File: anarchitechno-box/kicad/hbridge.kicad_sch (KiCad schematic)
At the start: 16 parts, among them U11 DRV8243SQDGQRQ1

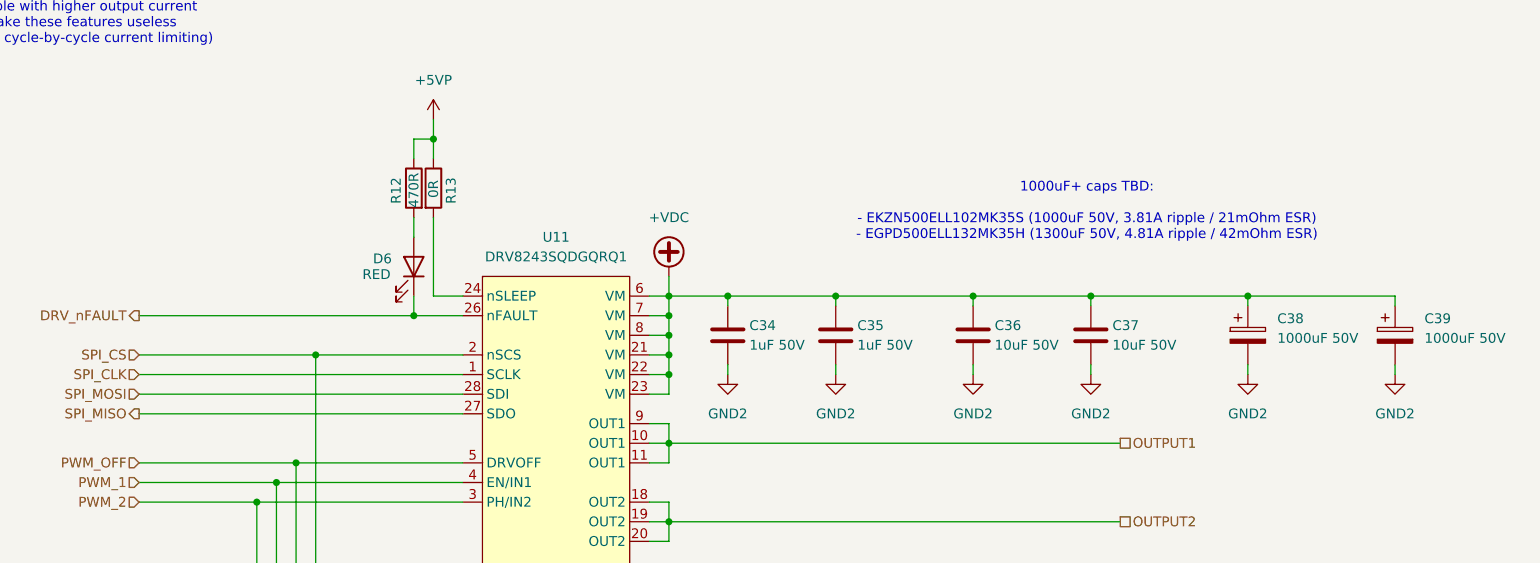
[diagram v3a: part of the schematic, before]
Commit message: Schematic & PCB changes: - Cleaned up unnecessary electrolytic input capacitor flyback - Removed dual diode rectification on 5V, increased output capacitors - Feedback resistors DC/DCs set, enlarged for JLC basic parts - Sweep through schematic to consolidate caps to JLC basic parts (see list schematic front page) - Midi OUTPUT added (please check schematic) - Wiznet W5500 schematic reworked to RJ45 reference schematic: https://docs.wiznet.io/assets/files/w5500_sch_v110_use_mag_-dfff8bbb103d13be4f25cd2b2f8b950d.pdf - Replaced ethernet jack to HR911105A - Crystals chosen for W5500 and RP2350B (according to reference), 15pF load caps. - RS485 driver changed to SP3485EN for 3.3V operation - Replaced RS485 bus connectors with 2x RJ45s for passthrough - Groove connector replaced with JST XH 2mm - Added LCSC part numbers for various components in the schematic
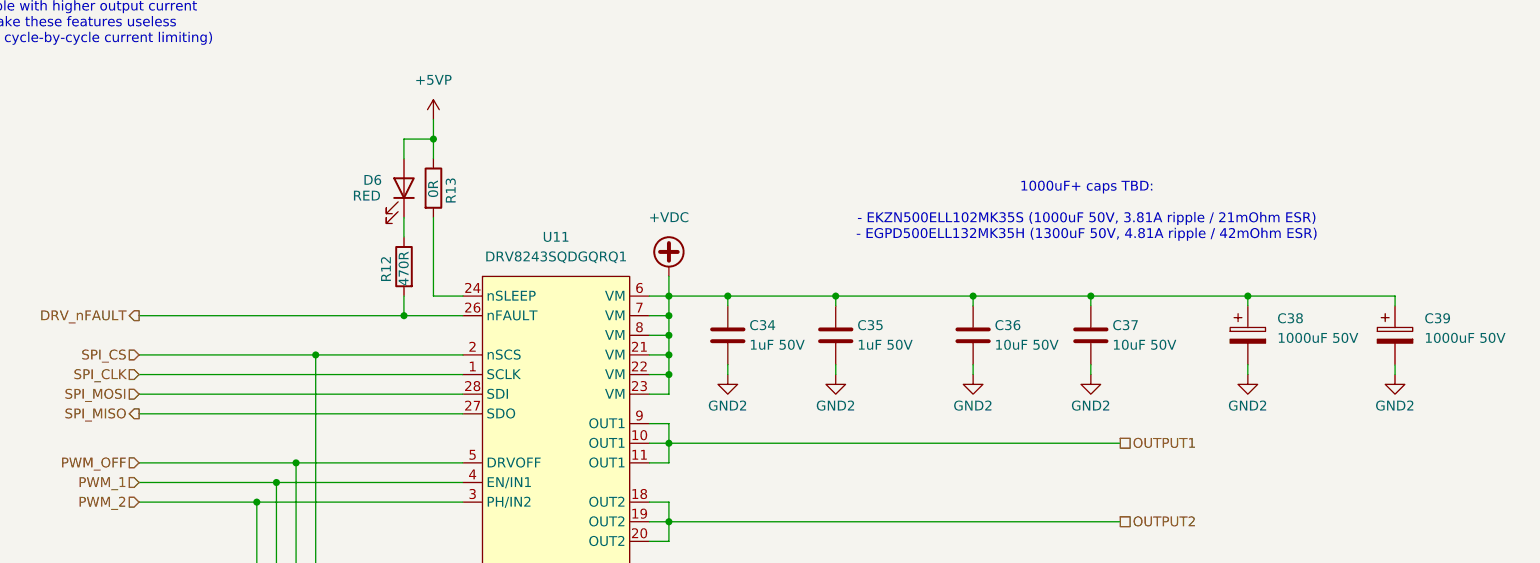
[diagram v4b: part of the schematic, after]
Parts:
- C34, C35: LCSC Part (none) -> C15849
- C36, C37: LCSC Part (none) -> C13585
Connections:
- net +5VP: now also D6.2 (A); no longer R12.1
- net DRV_nFAULT: now also R12.2; no longer D6.1 (K)
- new net: D6.1 (K), R12.1
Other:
- moved on the sheet: D6, R12
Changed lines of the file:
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@@
-	)
-	(junction
-		(at 111.76 69.85)
-		(diameter 0)
-		(color 0 0 0 0)
 	)
 	(junction
@@
 	)
 	(junction
+		(at 110.49 69.85)
+		(diameter 0)
+		(color 0 0 0 0)
+	)
+	(junction
 		(at 152.4 67.31)
 		(diameter 0)
@@
 	(wire
 		(pts
-			(xy 111.76 49.53) (xy 111.76 46.99)
-		)
-		(stroke
-			(width 0)
-			(type default)
-		)
-	)
-	(wire
-		(pts
 			(xy 144.78 83.82) (xy 144.78 86.36)
 		)
@@
 	(wire
 		(pts
+			(xy 110.49 69.85) (xy 118.11 69.85)
+		)
+		(stroke
+			(width 0)
+			(type default)
+		)
+	)
+	(wire
+		(pts
 			(xy 144.78 96.52) (xy 203.2 96.52)
 		)
@@
 	(wire
 		(pts
-			(xy 118.11 69.85) (xy 111.76 69.85)
-		)
-		(stroke
-			(width 0)
-			(type default)
-		)
-	)
-	(wire
-		(pts
 			(xy 238.76 67.31) (xy 219.71 67.31)
 		)
@@
 	(wire
 		(pts
+			(xy 110.49 49.53) (xy 110.49 46.99)
+		)
+		(stroke
+			(width 0)
+			(type default)
+		)
+	)
+	(wire
+		(pts
 			(xy 118.11 104.14) (xy 114.3 104.14)
 		)
@@
 	(wire
 		(pts
-			(xy 111.76 69.85) (xy 111.76 67.31)
-		)
-		(stroke
-			(width 0)
-			(type default)
-		)
-	)
-	(wire
-		(pts
 			(xy 99.06 110.49) (xy 99.06 74.93)
 		)
@@
 	(wire
 		(pts
-			(xy 76.2 69.85) (xy 111.76 69.85)
+			(xy 76.2 69.85) (xy 110.49 69.85)
+		)
+		(stroke
+			(width 0)
+			(type default)
+		)
+	)
+	(wire
+		(pts
+			(xy 110.49 57.15) (xy 110.49 59.69)
 		)
 		(stroke
@@
 	(wire
 		(pts
-			(xy 111.76 59.69) (xy 111.76 57.15)
-		)
-		(stroke
-			(width 0)
-			(type default)
-		)
-	)
-	(wire
-		(pts
 			(xy 144.78 111.76) (xy 144.78 114.3)
 		)
@@
 	(wire
 		(pts
+			(xy 110.49 46.99) (xy 114.3 46.99)
+		)
+		(stroke
+			(width 0)
+			(type default)
+		)
+	)
+	(wire
+		(pts
 			(xy 142.24 119.38) (xy 144.78 119.38)
 		)
@@
 	(wire
 		(pts
+			(xy 110.49 67.31) (xy 110.49 69.85)
+		)
+		(stroke
+			(width 0)
+			(type default)
+		)
+	)
+	(wire
+		(pts
 			(xy 142.24 116.84) (xy 144.78 116.84)
 		)
@@
 		(pts
 			(xy 144.78 77.47) (xy 144.78 74.93)
-		)
-		(stroke
-			(width 0)
-			(type default)
-		)
-	)
-	(wire
-		(pts
-			(xy 111.76 46.99) (xy 114.3 46.99)
 		)
 		(stroke
@@
 		(on_board yes)
 		(dnp no)
-		(fields_autoplaced yes)
 		(property "Reference" "#PWR076"
 			(at 199.39 83.82 0)
@@
 		)
 		(property "Value" "GND2"
-			(at 199.39 82.55 0)
+			(at 199.39 81.534 0)
 			(effects
 				(font
@@
 			)
 		)
+		(property "LCSC Part" "C13585"
+			(at 199.39 72.39 0)
+			(effects
+				(font
+					(size 1.27 1.27)
+				)
+				(hide yes)
+			)
+		)
 		(pin "2"
 		)
@@
 		(on_board yes)
 		(dnp no)
-		(fields_autoplaced yes)
 		(property "Reference" "#PWR077"
 			(at 219.71 83.82 0)
@@
 		)
 		(property "Value" "GND2"
-			(at 219.71 82.55 0)
+			(at 219.71 81.534 0)
 			(effects
 				(font
@@
 		)
 		(property "Description" "Unpolarized capacitor"
+			(at 152.4 72.39 0)
+			(effects
+				(font
+					(size 1.27 1.27)
+				)
+				(hide yes)
+			)
+		)
+		(property "LCSC Part" "C15849"
 			(at 152.4 72.39 0)
 			(effects
@@
 	(symbol
 		(lib_id "Device:R")
-		(at 111.76 53.34 0)
+		(at 110.49 63.5 0)
 		(mirror y)
 		(unit 1)
@@
 		(dnp no)
 		(property "Reference" "R12"
-			(at 109.474 55.372 90)
+			(at 108.204 65.532 90)
 			(effects
 				(font
@@
 		)
 		(property "Value" "470R"
-			(at 111.76 55.88 90)
+			(at 110.49 66.04 90)
 			(effects
 				(font
@@
 		)
 		(property "Footprint" "Resistor_SMD:R_0402_1005Metric"
-			(at 113.538 53.34 90)
+			(at 112.268 63.5 90)
 			(effects
 				(font
@@
 		)
 		(property "Datasheet" "~"
-			(at 111.76 53.34 0)
+			(at 110.49 63.5 0)
 			(effects
 				(font
@@
 		)
 		(property "Description" "Resistor"
-			(at 111.76 53.34 0)
+			(at 110.49 63.5 0)
 			(effects
 				(font
@@
 		(on_board yes)
 		(dnp no)
-		(fields_autoplaced yes)
 		(property "Reference" "#PWR078"
 			(at 238.76 83.82 0)
@@
 		)
 		(property "Value" "GND2"
-			(at 238.76 82.55 0)
+			(at 238.76 81.534 0)
 			(effects
 				(font
@@
 		(on_board yes)
 		(dnp no)
-		(fields_autoplaced yes)
 		(property "Reference" "#PWR073"
 			(at 152.4 83.82 0)
@@
 		)
 		(property "Value" "GND2"
-			(at 152.4 82.55 0)
+			(at 152.4 81.534 0)
 			(effects
 				(font
@@
 			)
 		)
+		(property "LCSC Part" "C15849"
+			(at 166.37 72.39 0)
+			(effects
+				(font
+					(size 1.27 1.27)
+				)
+				(hide yes)
+			)
+		)
 		(pin "2"
 		)
@@
 		(on_board yes)
 		(dnp no)
-		(fields_autoplaced yes)
 		(property "Reference" "#PWR075"
 			(at 184.15 83.82 0)
@@
 		)
 		(property "Value" "GND2"
-			(at 184.15 82.55 0)
+			(at 184.15 81.534 0)
 			(effects
 				(font
@@
 		(on_board yes)
 		(dnp no)
-		(fields_autoplaced yes)
 		(property "Reference" "#PWR074"
 			(at 166.37 83.82 0)
@@
 		)
 		(property "Value" "GND2"
-			(at 166.37 82.55 0)
+			(at 166.37 81.534 0)
 			(effects
 				(font
@@
 			)
 		)
+		(property "LCSC Part" "C13585"
+			(at 184.15 72.39 0)
+			(effects
+				(font
+					(size 1.27 1.27)
+				)
+				(hide yes)
+			)
+		)
 		(pin "2"
 		)
@@
 	(symbol
 		(lib_id "Device:LED")
-		(at 111.76 63.5 270)
+		(at 110.49 53.34 270)
 		(mirror x)
 		(unit 1)
@@
 		(dnp no)
 		(property "Reference" "D6"
-			(at 107.696 62.484 90)
+			(at 106.426 52.324 90)
 			(effects
 				(font
@@
 		)
 		(property "Value" "RED"
-			(at 106.934 64.516 90)
+			(at 105.664 54.356 90)
 			(effects
 				(font
@@
 		)
 		(property "Footprint" "LED_SMD:LED_0603_1608Metric"
-			(at 111.76 63.5 0)
+			(at 110.49 53.34 0)
 			(effects
 				(font
@@
 		)
 		(property "Datasheet" "~"
-			(at 111.76 63.5 0)
+			(at 110.49 53.34 0)
 			(effects
 				(font
@@
 		)
 		(property "Description" "Light emitting diode"
-			(at 111.76 63.5 0)
+			(at 110.49 53.34 0)
 			(effects
 				(font
@@
 		)
 		(property "Sim.Pins" "1=K 2=A"
-			(at 111.76 63.5 0)
-			(effects
-				(font
+			(at 110.49 53.34 0)
+			(effects
+				(font

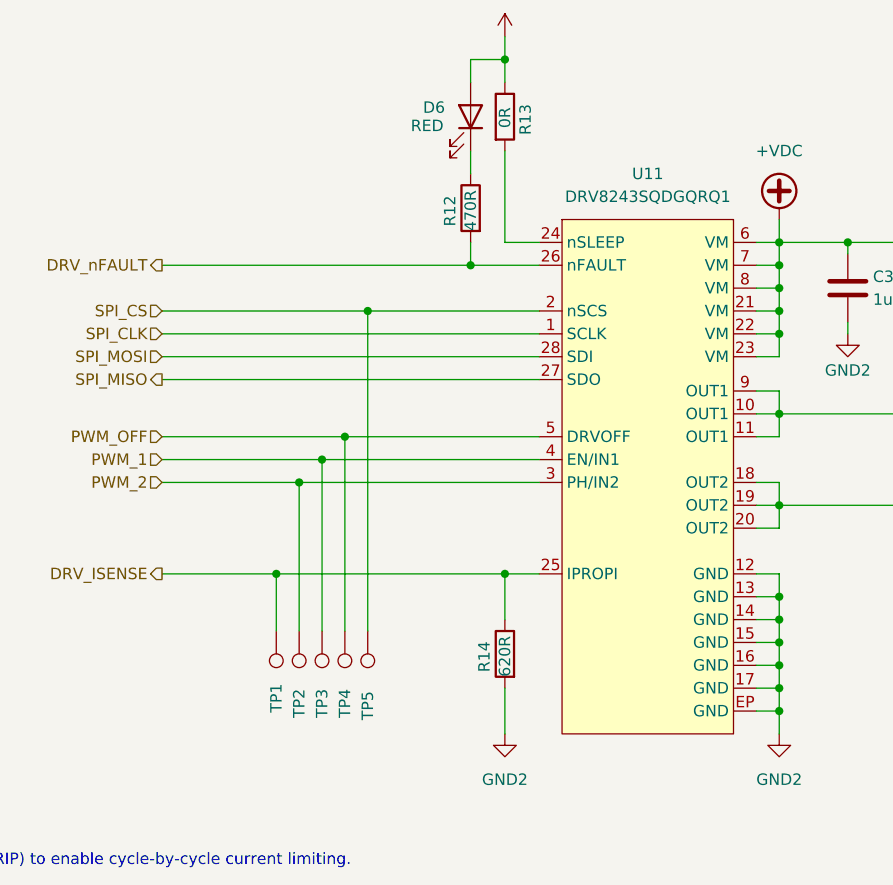
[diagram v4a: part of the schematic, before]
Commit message: - Thermische berekening DRV8245 vs losse transistors - DRV8245 package gecorrigeerd naar TSSOP-28 - Layout aangepast om grotere package te passen - 1x GND output per kanaal - Waarschijnlijk geen 140mm fan nodig => print weer gekropmen - RS485 power line gefixed (3.3V vs 3V3P) - Kleine BOM en I/O wijzigingen tbv layout
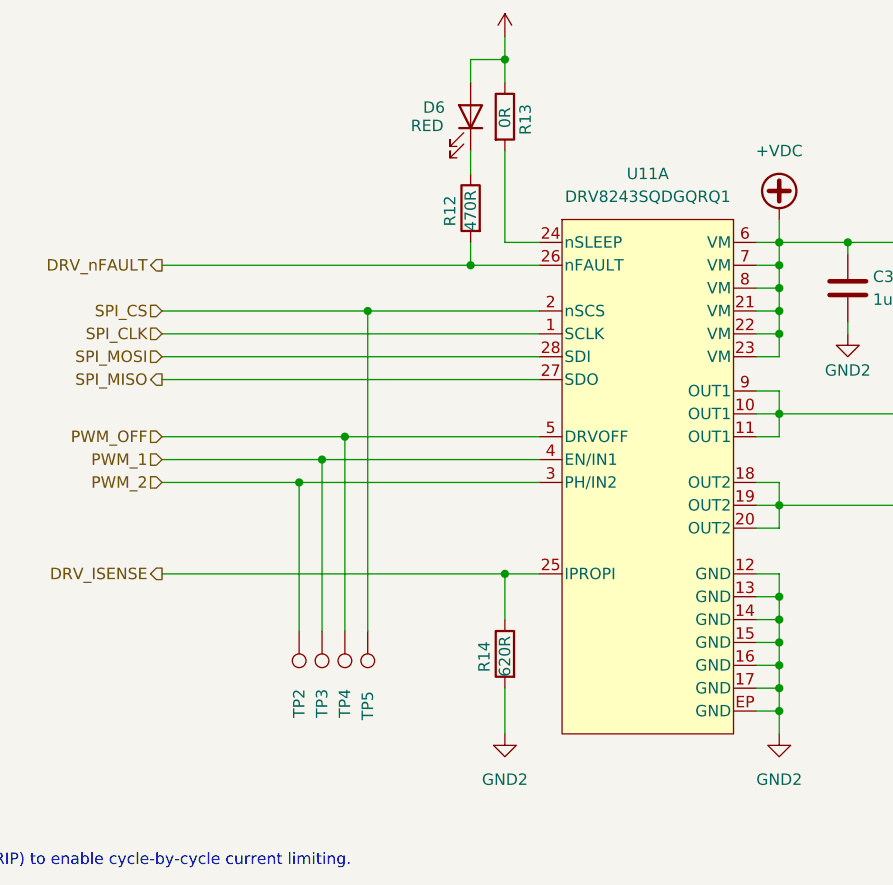
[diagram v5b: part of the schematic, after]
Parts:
- removed TP1: TestPoint, TestPoint:TestPoint_Pad_D1.0mm, symbol Connector:TestPoint
- U11: footprint parts:TI_HVSSOP-28 -> parts:TI_HTSSOP-28-M; symbol parts:DRV8243SQDGQRQ1 -> parts:DRV8245SQPWPRQ1; MPN DRV8243SQDGQRQ1 -> DRV8245SQPWPRQ1
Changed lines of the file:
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@@
-	)
-	(junction
-		(at 88.9 104.14)
-		(diameter 0)
-		(color 0 0 0 0)
 	)
 	(junction
@@
 	(wire
 		(pts
-			(xy 88.9 110.49) (xy 88.9 104.14)
-		)
-		(stroke
-			(width 0)
-			(type default)
-		)
-	)
-	(wire
-		(pts
 			(xy 144.78 111.76) (xy 144.78 114.3)
 		)
@@
 	(wire
 		(pts
-			(xy 88.9 104.14) (xy 114.3 104.14)
-		)
-		(stroke
-			(width 0)
-			(type default)
-		)
-	)
-	(wire
-		(pts
 			(xy 152.4 67.31) (xy 166.37 67.31)
 		)
@@
 	(wire
 		(pts
-			(xy 76.2 104.14) (xy 88.9 104.14)
+			(xy 76.2 104.14) (xy 114.3 104.14)
 		)
 		(stroke
@@
 	)
 	(symbol
-		(lib_id "parts:DRV8243SQDGQRQ1")
+		(lib_id "parts:DRV8245SQPWPRQ1")
 		(at 120.65 64.77 0)
 		(unit 1)
@@
 			)
 		)
-		(property "Footprint" "parts:TI_HVSSOP-28"
+		(property "Footprint" "parts:TI_HTSSOP-28-M"
+			(at 130.048 125.222 0)
+			(effects
+				(font
+					(size 1.27 1.27)
+					(italic yes)
+				)
+				(hide yes)
+			)
+		)
+		(property "Datasheet" "https://www.ti.com/lit/gpn/drv8245-q1"
+			(at 130.048 125.222 0)
+			(effects
+				(font
+					(size 1.27 1.27)
+					(italic yes)
+				)
+				(hide yes)
+			)
+		)
+		(property "Description" "Automotive H-Bridge Driver with Integrated Current Sense and Diagnostics"
 			(at 120.65 64.77 0)
 			(effects
@@
 			)
 		)
-		(property "Datasheet" "https://www.ti.com/lit/ds/symlink/drv8243-q1.pdf"
-			(at 146.05 126.746 0)
-			(effects
-				(font
-					(size 1.27 1.27)
-				)
-				(hide yes)
-			)
-		)
-		(property "Description" "Automotive H-Bridge Driver with Integrated Current Sense and Diagnostics"
-			(at 157.226 129.286 0)
-			(effects
-				(font
-					(size 1.27 1.27)
-				)
-				(hide yes)
-			)
-		)
-		(property "MPN" "DRV8243SQDGQRQ1"
-			(at 130.302 124.46 0)
+		(property "MPN" "DRV8245SQPWPRQ1"
+			(at 130.048 125.222 0)
 			(effects
 				(font
@@
 		)
 		(pin "21"
+		)
+		(pin "6"
+		)
+		(pin "7"
+		)
+		(pin "8"
+		)
+		(pin "21"
+		)
+		(pin "22"
+		)
+		(pin "23"
+		)
+		(pin "EPAD"
+		)
+		(pin "12"
+		)
+		(pin "13"
+		)
+		(pin "14"
+		)
+		(pin "15"
+		)
+		(pin "16"
+		)
+		(pin "17"
 		)
 		(instances
@@
 					(unit 1)
 				)
-			)
-		)
-	)
-	(symbol
-		(lib_id "Connector:TestPoint")
-		(at 88.9 110.49 180)
-		(unit 1)
-		(exclude_from_sim no)
-		(in_bom yes)
-		(on_board yes)
-		(dnp no)
-		(property "Reference" "TP1"
-			(at 88.9 116.332 90)
-			(effects
-				(font
-					(size 1.27 1.27)
-				)
-				(justify left)
-			)
-		)
-		(property "Value" "TestPoint"
-			(at 86.36 113.792 90)
-			(effects
-				(font
-					(size 1.27 1.27)
-				)
-				(hide yes)
-			)
-		)
-		(property "Footprint" "TestPoint:TestPoint_Pad_D1.0mm"
-			(at 83.82 110.49 0)
-			(effects
-				(font
-					(size 1.27 1.27)
-				)
-				(hide yes)
-			)
-		)
-		(property "Datasheet" "~"
-			(at 83.82 110.49 0)
-			(effects
-				(font
-					(size 1.27 1.27)
-				)
-				(hide yes)
-			)
-		)
-		(property "Description" "test point"
-			(at 88.9 110.49 0)
-			(effects
-				(font
-					(size 1.27 1.27)
-				)
-				(hide yes)
-			)
-		)
-		(pin "1"
-		)
-		(instances
-			(project "anarchytechnobox"
-				(path "/8c734c41-38ed-40fc-83bd-134786dcfb35/48f260d8-d62f-49a9-8985-05fca65ac6cb/0c0607e4-80d3-46ba-8adb-76563a900b03"
-					(reference "TP16")
-					(unit 1)
-				)
-				(path "/8c734c41-38ed-40fc-83bd-134786dcfb35/48f260d8-d62f-49a9-8985-05fca65ac6cb/ec360df5-fff7-49b0-afa3-93c9754653a9"
-					(reference "TP11")
-					(unit 1)
-				)
-				(path "/8c734c41-38ed-40fc-83bd-134786dcfb35/f97c65ed-bb3f-4eb8-a2c6-056cc510b5f8/0c0607e4-80d3-46ba-8adb-76563a900b03"
-					(reference "TP6")
-					(unit 1)
-				)
-				(path "/8c734c41-38ed-40fc-83bd-134786dcfb35/f97c65ed-bb3f-4eb8-a2c6-056cc510b5f8/ec360df5-fff7-49b0-afa3-93c9754653a9"
-					(reference "TP1")
-					(unit 1)
-				)

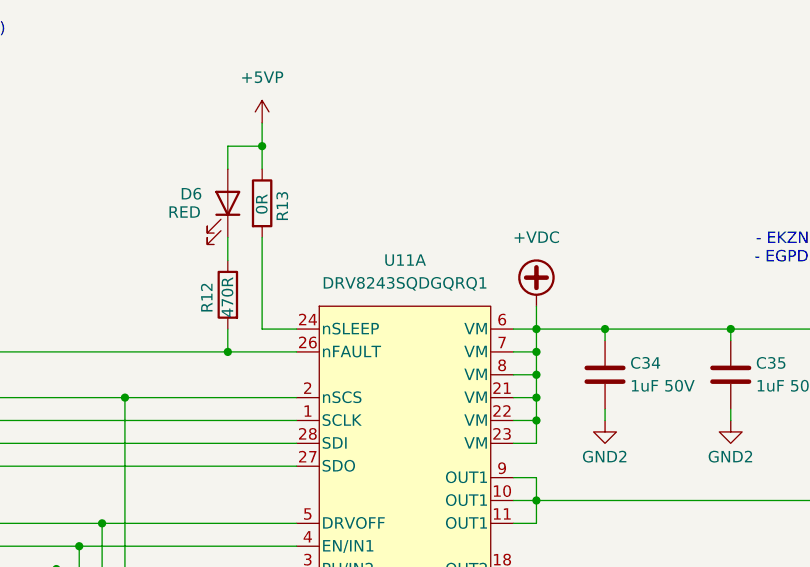
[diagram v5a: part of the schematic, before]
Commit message: BOM nagelopen, bestelklaar.
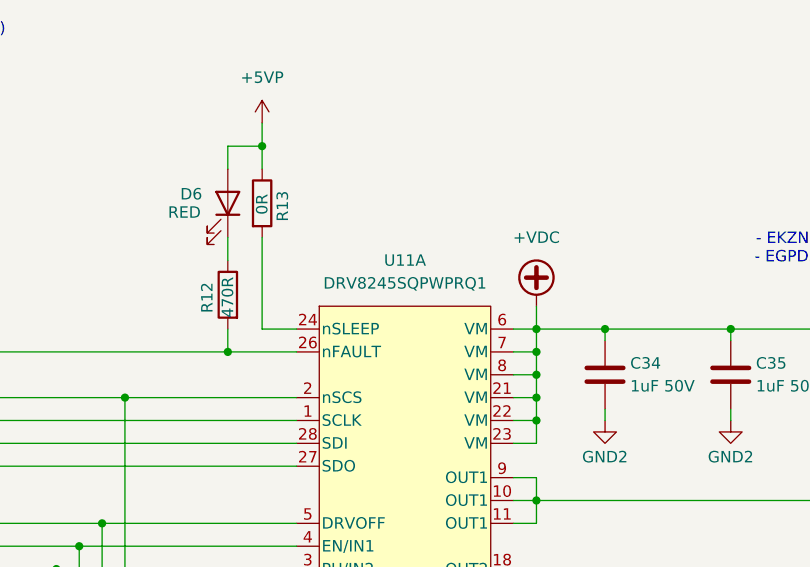
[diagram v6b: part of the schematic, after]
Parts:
- C38, C39: LCSC Part (none) -> C443023
- TP2, TP3, TP4, TP5: now left out of the parts list
- U11: value DRV8243SQDGQRQ1 -> DRV8245SQPWPRQ1; LCSC Part (none) -> C5672500
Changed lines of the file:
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@@
 			)
 		)
-		(property "Value" "DRV8243SQDGQRQ1"
+		(property "Value" "DRV8245SQPWPRQ1"
 			(at 130.175 62.23 0)
 			(effects
@@
 			)
 		)
+		(property "LCSC Part" "C5672500"
+			(at 120.65 64.77 0)
+			(effects
+				(font
+					(size 1.27 1.27)
+				)
+				(hide yes)
+			)
+		)
 		(pin "19"
 		)
@@
 		(unit 1)
 		(exclude_from_sim no)
-		(in_bom yes)
+		(in_bom no)
 		(on_board yes)
 		(dnp no)
@@
 			)
 		)
+		(property "LCSC Part" "C443023"
+			(at 219.71 72.39 0)
+			(effects
+				(font
+					(size 1.27 1.27)
+				)
+				(hide yes)
+			)
+		)
 		(pin "2"
 		)
@@
 		(unit 1)
 		(exclude_from_sim no)
-		(in_bom yes)
+		(in_bom no)
 		(on_board yes)
 		(dnp no)
@@
 		(unit 1)
 		(exclude_from_sim no)
-		(in_bom yes)
+		(in_bom no)
 		(on_board yes)
 		(dnp no)
@@
 		(unit 1)
 		(exclude_from_sim no)
-		(in_bom yes)
+		(in_bom no)
 		(on_board yes)
 		(dnp no)
@@
 			(at 238.76 72.39 0)
 			(effects
+				(font
+					(size 1.27 1.27)
+				)
+				(hide yes)
+			)
+		)
+		(property "LCSC Part" "C443023"
+			(at 238.76 72.39 0)
+			(effects
